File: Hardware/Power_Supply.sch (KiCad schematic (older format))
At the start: 13 parts, among them U1 TPS565208DDC

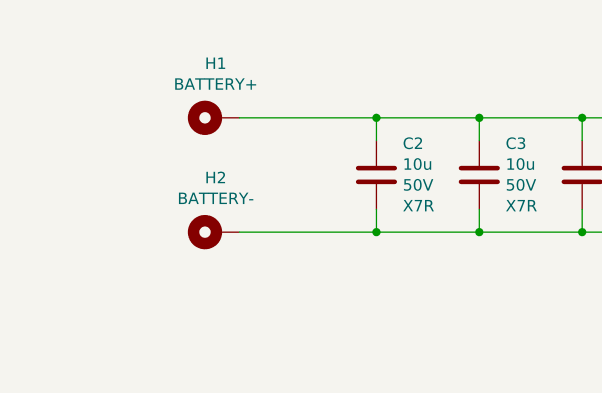
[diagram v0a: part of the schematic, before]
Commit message: [Hardware] Added a switch to turn off power supply.
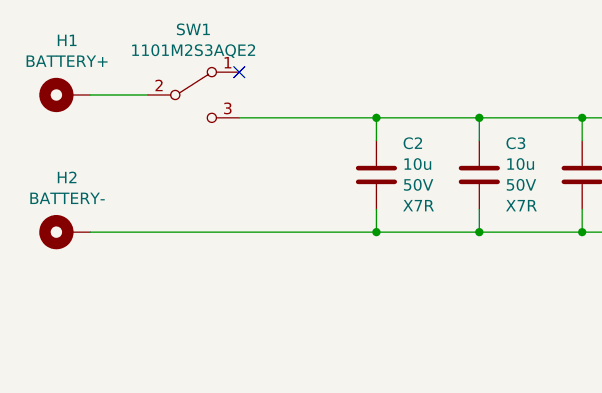
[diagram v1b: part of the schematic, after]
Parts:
- added SW1: 1101M2S3AQE2, 1101M2S3AQE2:1101M2S3AQE2, symbol Switch:SW_SPDT
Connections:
- net at C2.2, C3.2, C4.2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: now also SW1.3 (C); no longer H1.1
- new net: H1.1, SW1.2 (B)
- no-connect marks 0 -> 1
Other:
- moved on the sheet: H1, H2
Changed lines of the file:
@@
 L Mechanical:MountingHole_Pad H2
 U 1 1 5F1FE00E
-P 2900 3950
-F 0 "H2" V 3137 3953 50  0000 C CNN
-F 1 "BATTERY-" V 3046 3953 50  0000 C CNN
-F 2 "MountingHole:MountingHole_2.2mm_M2_Pad" H 2900 3950 50  0001 C CNN
-F 3 "~" H 2900 3950 50  0001 C CNN
-	1    2900 3950
+P 2250 3950
+F 0 "H2" V 2487 3953 50  0000 C CNN
+F 1 "BATTERY-" V 2396 3953 50  0000 C CNN
+F 2 "MountingHole:MountingHole_2.2mm_M2_Pad" H 2250 3950 50  0001 C CNN
+F 3 "~" H 2250 3950 50  0001 C CNN
+	1    2250 3950
 	0    -1   -1   0
 $EndComp
@@
 L Mechanical:MountingHole_Pad H1
 U 1 1 5F1FF3A5
-P 2900 3450
-F 0 "H1" V 3137 3453 50  0000 C CNN
-F 1 "BATTERY+" V 3046 3453 50  0000 C CNN
-F 2 "MountingHole:MountingHole_2.2mm_M2_Pad" H 2900 3450 50  0001 C CNN
-F 3 "~" H 2900 3450 50  0001 C CNN
-	1    2900 3450
+P 2250 3350
+F 0 "H1" V 2487 3353 50  0000 C CNN
+F 1 "BATTERY+" V 2396 3353 50  0000 C CNN
+F 2 "MountingHole:MountingHole_2.2mm_M2_Pad" H 2250 3350 50  0001 C CNN
+F 3 "~" H 2250 3350 50  0001 C CNN
+	1    2250 3350
 	0    -1   -1   0
 $EndComp
@@
 Connection ~ 4500 3950
 Wire Wire Line
-	3000 3950 3600 3950
+	2350 3950 3600 3950
 Connection ~ 3600 3950
 Wire Wire Line
@@
 Wire Wire Line
 	7250 3450 7550 3450
+$Comp
+L Switch:SW_SPDT SW1
+U 1 1 5F22069E
+P 2800 3350
+F 0 "SW1" H 2800 3635 50  0000 C CNN
+F 1 "1101M2S3AQE2" H 2800 3544 50  0000 C CNN
+F 2 "1101M2S3AQE2:1101M2S3AQE2" H 2800 3350 50  0001 C CNN
+F 3 "~" H 2800 3350 50  0001 C CNN
+	1    2800 3350
+	1    0    0    -1
+$EndComp
+Wire Wire Line
+	2350 3350 2600 3350
+NoConn ~ 3000 3250
 $EndSCHEMATC
